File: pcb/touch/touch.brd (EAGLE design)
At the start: 97.8 x 36.2 mm, 36 parts, among them U1 MPR084EJ, U2 PCA9533D/01

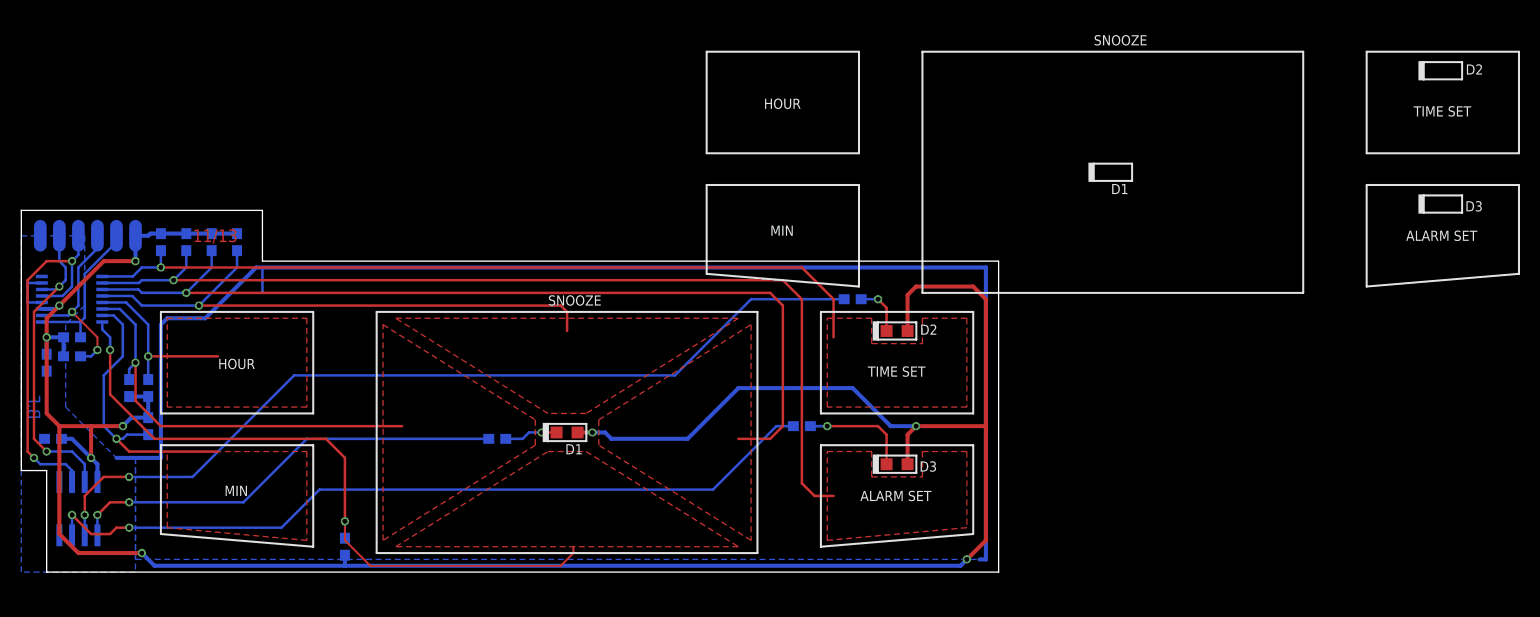
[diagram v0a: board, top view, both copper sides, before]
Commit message: Display base pcb (rev C), Touch panel (rev B)
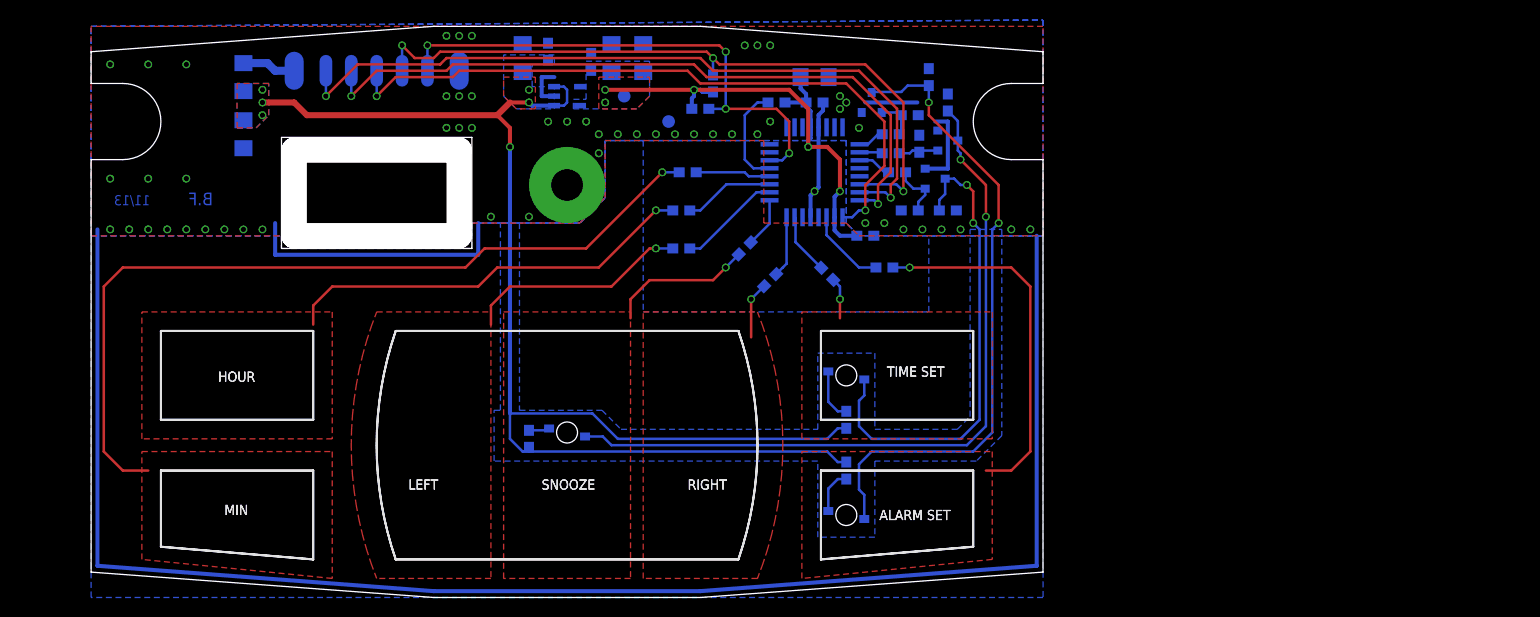
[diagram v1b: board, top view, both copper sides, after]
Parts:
- removed !ATTN: 2, Misc:WIRE_SMT
- removed !IRQ: 3, Misc:WIRE_SMT
- removed 3.3V: 1, Misc:WIRE_SMT
- removed SCL: 4, Misc:WIRE_SMT
- removed SDA: 5, Misc:WIRE_SMT
- removed U$1: (no value), Symbols:INFO_AUTHOR
- removed U$11, U$12, U$13, U$14, U$15, U$16: (no value), Symbols:LEGEND_ROW_30
- removed U$2: (no value), Symbols:INFO_DATE
- removed W6: 6, Misc:WIRE_SMT
- added !CHANGE: 2, Misc:WIRE_SMT_125X50
- added 5V: 7, Misc:WIRE_SMT_150X75
- added C10, C9: N/A, Passive:SMD_1206
- added C11, C12, C8: 100nF, Passive:SMD_0603
- added C3: 1uF, Passive:SMD_1206
- added C4, C5: 10nF, Passive:SMD_0603
- added C6, C7: 4.7uF, Passive:SMD_1206
- added CLK: 4, Misc:WIRE_SMT_125X50
- added CS: 3, Misc:WIRE_SMT_125X50
- added GND: 1, Misc:WIRE_SMT_150X75
- added MISO: 5, Misc:WIRE_SMT_125X50
- added MOSI: 6, Misc:WIRE_SMT_125X50
- added Q1, Q2, Q3: MMBT3904, Transistor:SOT23
- added R14, R15, R16, R17, R18, R20: 100k, Passive:SMD_0603
- added R19: 0, Passive:SMD_1206
- added TP1: VDD, Misc:TP_050
- added TP2: VSS, Misc:TP_050
- C1: value 1uF -> 10nF
- D1, D2, D3: device Optoelectronic:CHIPLED_0805 -> Optoelectronic:P47F
- R1, R2, R3, R4, R5, R6, R7: value 780k -> 10k
- R10, R9: value 4.7k -> 3k
- R11, R12, R13: value 56 -> 39
- R8: value 780k -> 3k
- U1: value MPR084EJ -> AT42QT1085-AU; device IC:TSSOP16 -> IC:TQFP-7X7-32
- U2: value PCA9533D/01 -> ADP150AUJZ-3.3-R7; device IC:SOIC8 -> Power:SOT23-5
- moved C1 93.9 mm to (38.1, 21.0)
- moved R10 84.6 mm to (33.0, 14.0), turned to 180 degrees
- moved R9 84.0 mm to (32.4, 15.9), turned to 180 degrees
- moved C2 83.3 mm to (24.8, 21.0), turned to 180 degrees
- moved R8 80.3 mm to (32.4, 17.8), turned to 180 degrees
- moved U1 75.4 mm to (24.8, 14.0), turned to 270 degrees
- moved R1 69.6 mm to (26.0, 3.81), turned to 225 degrees
- moved R7 64.8 mm to (31.8, 4.45), turned to 180 degrees
- moved U2 64.0 mm to (0.00, 21.6), turned to 90 degrees
- moved R2 63.2 mm to (20.3, 3.17), turned to 315 degrees
- moved R3 53.3 mm to (17.8, 6.35), turned to 315 degrees
- moved R5 52.2 mm to (11.4, 10.2), turned to 0 degrees
- moved R6 50.8 mm to (12.1, 14.0), turned to 0 degrees
- moved R4 49.5 mm to (11.4, 6.35), turned to 0 degrees
- moved U$5 32.5 mm to (-31.8, 11.4)
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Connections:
- removed net !ATTN: !ATTN.1, R9.1, U1.1
- removed net !IRQ: !IRQ.1, R10.1, U1.2
- removed net 3.3V: 3.3V.1, C1.2, C2.1, D1.A, D2.A, D3.A, R1.2, R10.2, R2.2, R3.2, R4.2, R5.2, R6.2, R7.2, R8.2, R9.2, U1.3, U2.8
- removed net E_DOWN: R6.1, U1.16
- removed net E_UP: R7.1, U1.12
- removed net SCL: SCL.1, U1.5, U2.6
- removed net SDA: SDA.1, U1.6, U2.7
- new net !CHANGE: !CHANGE.1, R15.1, U1.30
- new net 5V: C7.1, C8.1, C9.1, R11.2, R12.2, R13.2, R19.2, U2.1, U2.3
- new net CLK: CLK.1, U1.17
- new net CS: CS.1, R16.1, U1.14
- new net E_SNOOZE: R3.2
- new net LED_ALARM: R8.1, U1.9
- new net LED_SNOOZE: R9.1, U1.10
- new net LED_TIME: R10.1, U1.11
- new net MISO: MISO.1, U1.16
- new net MOSI: MOSI.1, U1.15
- new net N$10: R4.1, U1.26
- new net N$11: R5.1, U1.27
- new net N$12: R6.1, U1.28
- new net N$13: R7.1, U1.19
- new net N$14: Q3.1, R10.2, R14.2
- new net N$15: Q2.1, R18.2, R8.2
- new net N$16: Q1.1, R17.2, R9.2
- new net N$18: 5V.1, R19.1
- new net N$19: R20.1, U1.29
- new net N$7: R1.1, U1.23
- new net N$8: R2.1, U1.24
- new net N$9: R3.1, U1.25
- new net VDD: C10.1, C11.1, C12.1, C2.1, C3.1, C6.1, R15.2, R16.2, R20.2, TP1.1, U1.18, U1.4, U2.5
- net E_ALARM: now also R7.2; no longer R4.1, U1.10
- net E_HOUR: now also R5.2; no longer R2.1, U1.13
- net E_LEFT: now also R4.2; no longer R8.1, U1.14
- net E_MIN: now also R6.2; no longer R1.1, U1.15
- net E_RIGHT: now also R2.2; no longer R3.1, U1.11
- net E_TIME: now also R1.2; no longer R5.1, U1.9
- net GND: now also C1.2, C10.2, C11.2, C12.2, C3.2, C4.2, C5.2, C6.2, C7.2, C8.2, C9.2, GND.1, Q1.2, Q2.2, Q3.2, R14.1, R17.1, R18.1, TP2.1, U1.21, U1.5, U2.2; no longer C1.1, U1.4, U1.7, U2.4, W6.1
- net N$1: now also C1.1, Q1.3; no longer R11.2
- net N$2: now also C4.1, Q2.3; no longer R12.2
- net N$3: now also C5.1, Q3.3; no longer R13.2
- net N$4: now also D1.A; no longer U2.1
- net N$5: now also D2.A; no longer U2.2
- net N$6: now also D3.A; no longer U2.3
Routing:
- net 3.3V: track 257.7 -> 0.00 mm, vias 9 -> 0
- net 5V: track 0.00 -> 137.6 mm, vias 0 -> 6
- net E_RIGHT: track 91.1 -> 5.65 mm
- net N$5: track 88.1 -> 4.44 mm, vias 2 -> 0
- net GND: track 139.9 -> 217.4 mm, vias 0 -> 57
- net E_TIME: track 80.4 -> 4.12 mm
- net MOSI: track 0.00 -> 75.9 mm, vias 0 -> 2
- net N$6: track 79.5 -> 5.24 mm, vias 2 -> 0
- net MISO: track 0.00 -> 71.4 mm, vias 0 -> 2
- net CS: track 0.00 -> 70.9 mm, vias 0 -> 3
- net N$1: track 5.35 -> 74.4 mm, vias 1 -> 2
- net CLK: track 0.00 -> 68.7 mm, vias 0 -> 2
- net E_DOWN: track 68.7 -> 0.00 mm, vias 2 -> 0
- net E_ALARM: track 96.5 -> 36.3 mm
- net N$2: track 5.22 -> 64.2 mm, vias 1 -> 2
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- added copper zone on layer 1, net 5V
- added copper zone on layer 16, net 5V
- added copper zone on layer 1, net E_SNOOZE
- added copper zone on layer 1, net GND
- added copper zone on layer 16, net N$17
- added copper zone on layer 1, net VDD
- added copper zone on layer 16, net VDD
- removed copper zone on layer 1, net E_DOWN
- removed copper zone on layer 1, net E_UP
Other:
- board size 97.8 x 36.2 mm -> 95.2 x 57.1 mm
- board text added: "7"
- board text added: ">DATE"
- board text added: "B"
- board text added: "B.F"
- board text added: "C10"
- board text added: "C11"
- board text added: "C12"
- board text added: "C3"
- board text added: "C4"
- board text added: "C5"
- board text added: "C6"
- board text added: "C7"
- board text added: "C8"
- board text added: "C9"
- board text added: "LEFT"
- board text added: "Q1"
- board text added: "Q2"
- board text added: "Q3"
- board text added: "R14"
- board text added: "R15"
- board text added: "R16"
- board text added: "R17"
- board text added: "R18"
- board text added: "R19"
- board text added: "R20"
- board text added: "RIGHT"
- board text added: "TP1"
- board text added: "TP2"
- board text removed: "2"
- board text removed: "3"
- board text removed: "3.3V"
- board text removed: "4"
- board text removed: "5"
- board text removed: "6"
- board text removed: "A"
- board text removed: "ATTN"
- board text removed: "GND"
- board text removed: "IRQ"
- board text removed: "SCL"
- board text removed: "SDA"

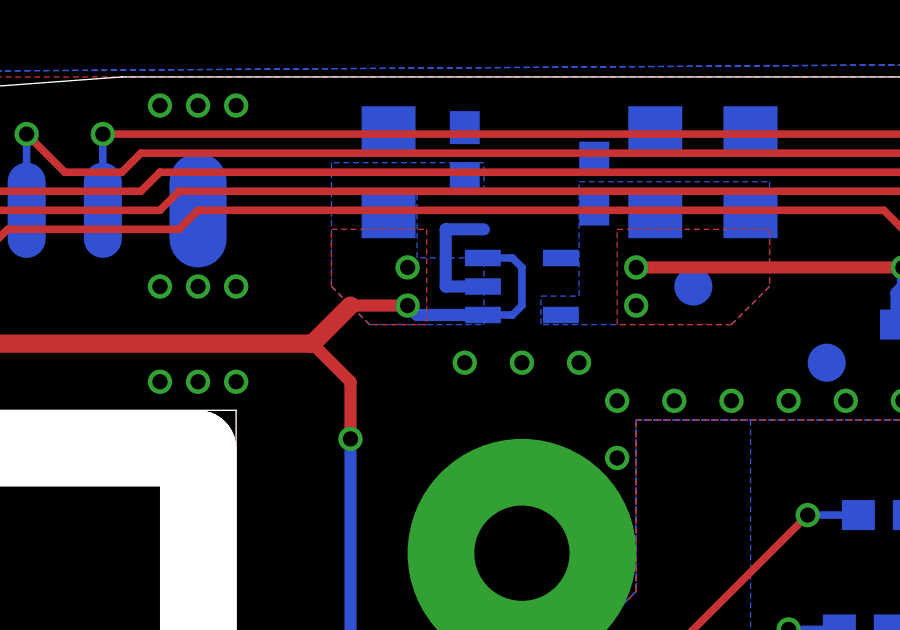
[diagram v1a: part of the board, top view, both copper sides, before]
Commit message: Changed page format on schematics to US letter (8.5" x 11")
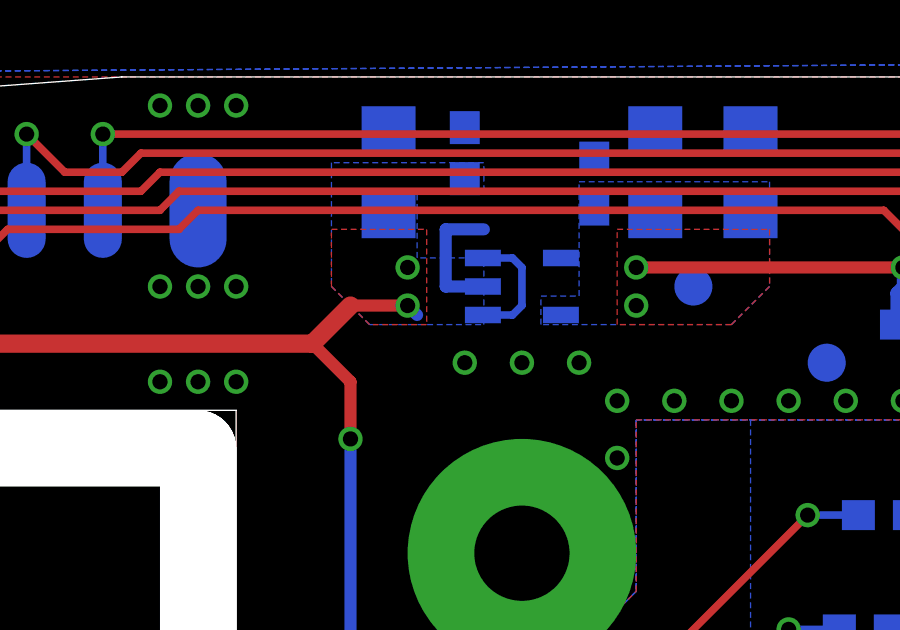
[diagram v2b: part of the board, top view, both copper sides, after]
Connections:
- net VDD renamed VDD_TOUCH
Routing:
- net 5V: track 137.6 -> 135.4 mm
